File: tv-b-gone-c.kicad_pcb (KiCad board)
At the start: 2 copper layers, 24 x 28.6 mm, 28 parts, among them J2 USB4515, Q1 MMBT3904, Q2 MMBT3904, Q3 MMBT3904, Q4 MMBT3904, Q5 MMBT2907A, U1 ATtiny85V-10S, Y1 8MHz

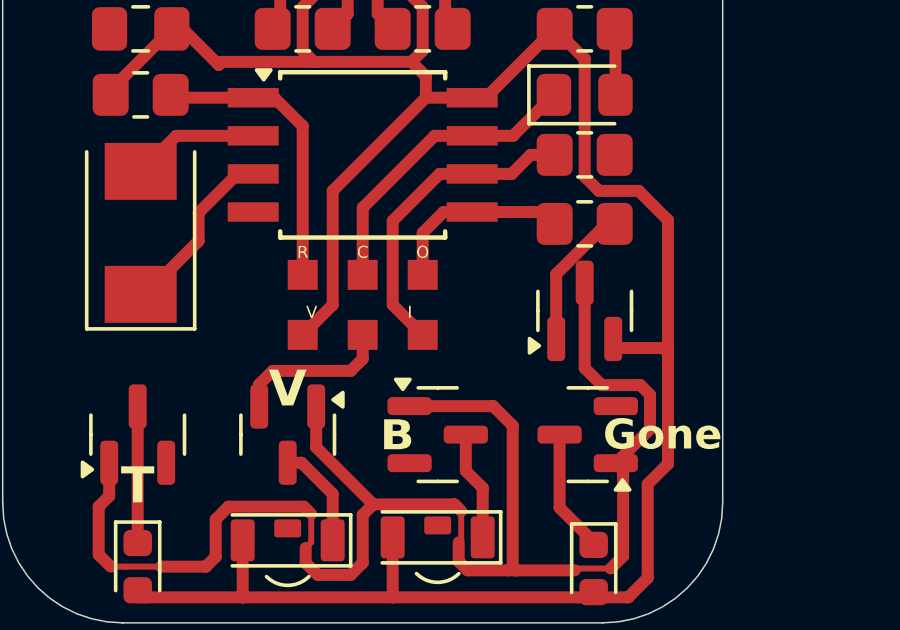
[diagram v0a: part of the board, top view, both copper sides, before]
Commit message: Update values post-fab, fix trace
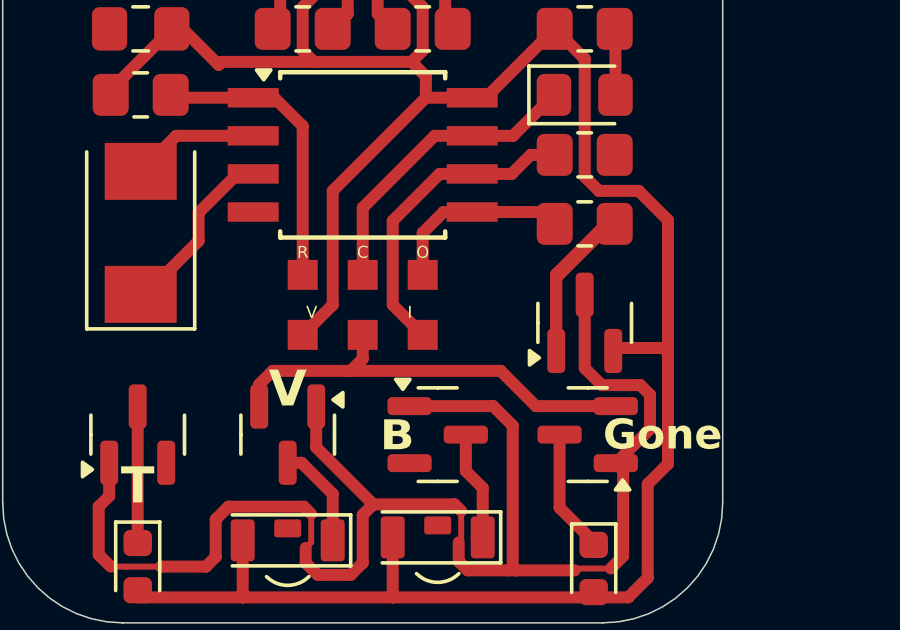
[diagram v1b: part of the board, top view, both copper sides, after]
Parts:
- C1: value C -> 100n
- R1: value 10k -> 100
- R3: value R -> ~680
- moved Q5 0.40 mm to (107.4, 63.0)
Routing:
- net GND: track 10.1 -> 19.6 mm
- net Net-(Q5-B): track 5.11 -> 10.2 mm

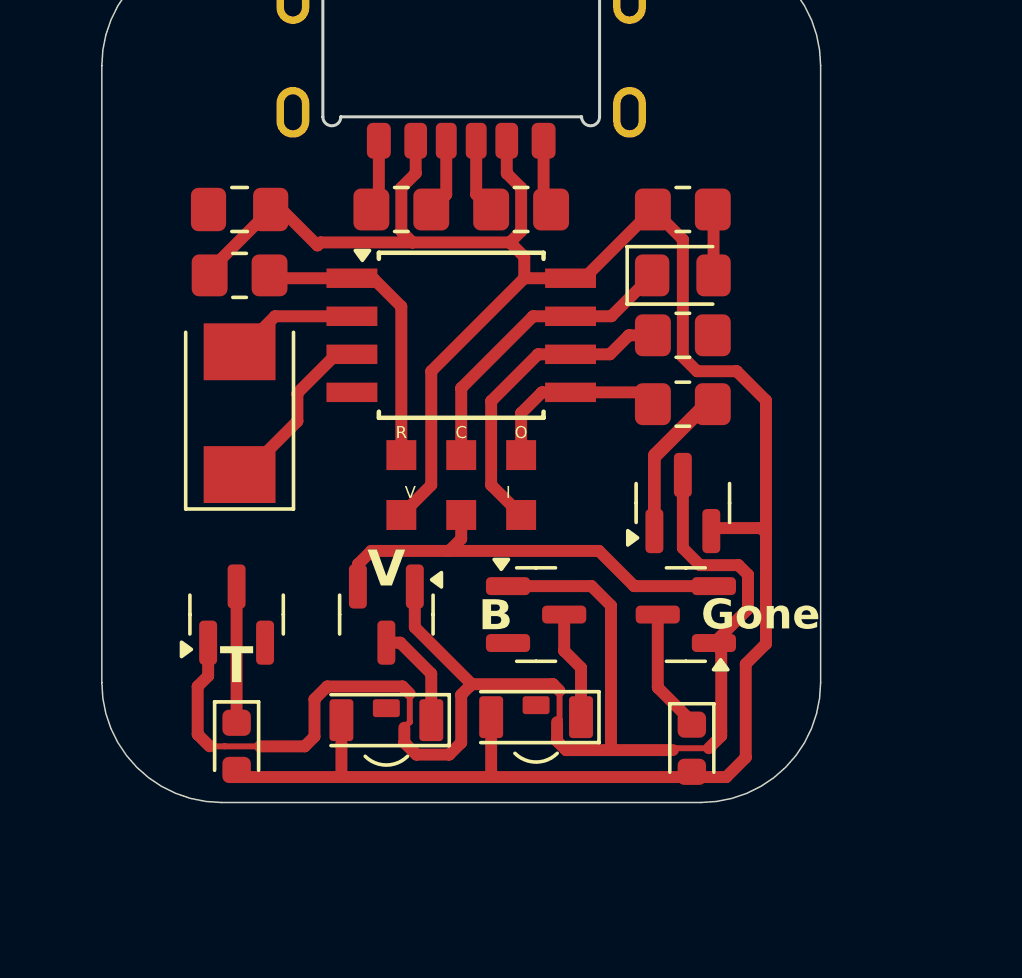
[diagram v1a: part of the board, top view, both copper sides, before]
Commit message: Add reset button, use mosfet
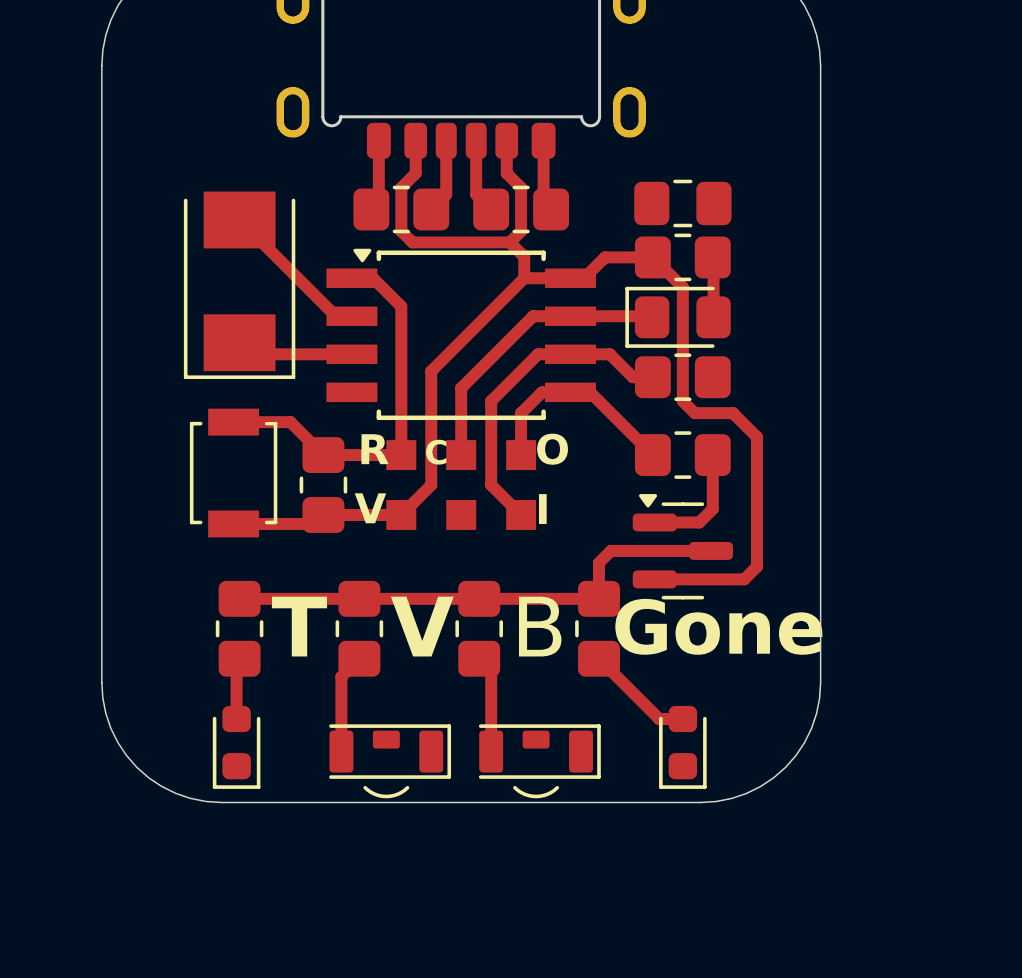
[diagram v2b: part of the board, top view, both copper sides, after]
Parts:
- removed Q1, Q2, Q3, Q4: MMBT3904, Package_TO_SOT_SMD:SOT-23
- added R10: 100, Resistor_SMD:R_0805_2012Metric_Pad1.20x1.40mm_HandSolder, F.Cu at (104.6, 67.2)
- added R7: 100, Resistor_SMD:R_0805_2012Metric_Pad1.20x1.40mm_HandSolder, F.Cu at (92.6, 67.2)
- added R8: 100, Resistor_SMD:R_0805_2012Metric_Pad1.20x1.40mm_HandSolder, F.Cu at (96.6, 67.2)
- added R9: 100, Resistor_SMD:R_0805_2012Metric_Pad1.20x1.40mm_HandSolder, F.Cu at (100.6, 67.2)
- added SW1: SW_SPST, Button_Switch_SMD:SW_SPST_B3U-1000P, F.Cu at (92.4, 62.0)
- R3: value ~680 -> min. 680
- moved C1 14.8 mm to (107.4, 53.0)
- moved R4 7.54 mm to (95.4, 62.4), turned to 90 degrees
- moved Y1 4.40 mm to (92.6, 55.6)
- moved R1 1.70 mm to (107.4, 61.4)
- moved Q5 1.60 mm to (107.4, 64.6), turned to 0 degrees
- moved R3 1.60 mm to (107.4, 54.8)
- moved D1 1.40 mm to (107.4, 56.8)
- moved R2 1.40 mm to (107.4, 58.8)
- moved D5 1.15 mm to (102.5, 71.2)
- moved D2 1.05 mm to (97.5, 71.2)
- moved D4 0.35 mm to (107.4, 71.0), turned to 90 degrees
- moved D3 0.12 mm to (92.5, 71.0), turned to 90 degrees
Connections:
- D2 pad 1: Net-(D2-K) -> GND
- D2 pad 2: +5V -> Net-(D2-A)
- D3 pad 1: Net-(D3-K) -> GND
- D3 pad 2: +5V -> Net-(D3-A)
- D4 pad 1: Net-(D4-K) -> GND
- D4 pad 2: +5V -> Net-(D4-A)
- D5 pad 1: Net-(D5-K) -> GND
- D5 pad 2: +5V -> Net-(D5-A)
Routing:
- net Net-(Q5-C): track 52.4 -> 17.9 mm
- net +5V: track 77.8 -> 48.2 mm
- net GND: track 19.6 -> 4.80 mm
- net Net-(Q5-B): track 10.2 -> 3.92 mm
- net Net-(D3-K): track 4.31 -> 0.00 mm
- net Net-(D5-K): track 3.91 -> 0.00 mm
- net Net-(D4-K): track 3.76 -> 0.00 mm
- net Net-(D4-A): track 0.00 -> 3.63 mm
- net Net-(D2-K): track 3.48 -> 0.00 mm
- net Net-(D2-A): track 0.00 -> 3.35 mm
- net /~{RST}: track 9.79 -> 13.1 mm
- net Net-(D5-A): track 0.00 -> 3.27 mm
- net Net-(U1-XTAL2/PB4): track 5.96 -> 3.91 mm
- net Net-(D3-A): track 0.00 -> 1.65 mm
- net Net-(U1-XTAL1/PB3): track 4.24 -> 5.08 mm
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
